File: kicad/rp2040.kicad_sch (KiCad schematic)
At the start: 0 parts

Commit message: w5500 ethernet schematic
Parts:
- added U1: RP2040, Package_DFN_QFN:QFN-56-1EP_7x7mm_P0.4mm_EP3.2x3.2mm, symbol MCU_RaspberryPi:RP2040
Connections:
- new net: U1.1 (IOVDD), U1.10 (IOVDD), U1.22 (IOVDD), U1.33 (IOVDD), U1.42 (IOVDD), U1.49 (IOVDD)
- new net: U1.23 (DVDD), U1.50 (DVDD)
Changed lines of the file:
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@@
 	(generator_version "9.0")
 	(paper "A4")
+	(symbol
+		(lib_id "MCU_RaspberryPi:RP2040")
+		(at 144.78 97.79 0)
+		(unit 1)
+		(exclude_from_sim no)
+		(in_bom yes)
+		(on_board yes)
+		(dnp no)
+		(fields_autoplaced yes)
+		(property "Reference" "U1"
+			(at 146.9233 142.24 0)
+			(effects
+				(font
+					(size 1.27 1.27)
+				)
+				(justify left)
+			)
+		)
+		(property "Value" "RP2040"
+			(at 146.9233 144.78 0)
+			(effects
+				(font
+					(size 1.27 1.27)
+				)
+				(justify left)
+			)
+		)
+		(property "Footprint" "Package_DFN_QFN:QFN-56-1EP_7x7mm_P0.4mm_EP3.2x3.2mm"
+			(at 144.78 97.79 0)
+			(effects
+				(font
+					(size 1.27 1.27)
+				)
+				(hide yes)
+			)
+		)
+		(property "Datasheet" "https://datasheets.raspberrypi.com/rp2040/rp2040-datasheet.pdf"
+			(at 144.78 97.79 0)
+			(effects
+				(font
+					(size 1.27 1.27)
+				)
+				(hide yes)
+			)
+		)
+		(property "Description" "A microcontroller by Raspberry Pi"
+			(at 144.78 97.79 0)
+			(effects
+				(font
+					(size 1.27 1.27)
+				)
+				(hide yes)
+			)
+		)
+		(pin "32"
+		)
+		(pin "12"
+		)
+		(pin "13"
+		)
+		(pin "41"
+		)
+		(pin "22"
+		)
+		(pin "9"
+		)
+		(pin "17"
+		)
+		(pin "5"
+		)
+		(pin "19"
+		)
+		(pin "11"
+		)
+		(pin "14"
+		)
+		(pin "7"
+		)
+		(pin "8"
+		)
+		(pin "16"
+		)
+		(pin "50"
+		)
+		(pin "23"
+		)
+		(pin "57"
+		)
+		(pin "4"
+		)
+		(pin "46"
+		)
+		(pin "56"
+		)
+		(pin "53"
+		)
+		(pin "55"
+		)
+		(pin "54"
+		)
+		(pin "31"
+		)
+		(pin "15"
+		)
+		(pin "29"
+		)
+		(pin "10"
+		)
+		(pin "43"
+		)
+		(pin "1"
+		)
+		(pin "28"
+		)
+		(pin "45"
+		)
+		(pin "47"
+		)
+		(pin "26"
+		)
+		(pin "52"
+		)
+		(pin "51"
+		)
+		(pin "24"
+		)
+		(pin "33"
+		)
+		(pin "36"
+		)
+		(pin "35"
+		)
+		(pin "2"
+		)
+		(pin "20"
+		)
+		(pin "21"
+		)
+		(pin "3"
+		)
+		(pin "38"
+		)
+		(pin "27"
+		)
+		(pin "37"
+		)
+		(pin "18"
+		)
+		(pin "48"
+		)
+		(pin "6"
+		)
+		(pin "39"
+		)
+		(pin "34"
+		)
+		(pin "30"
+		)
+		(pin "42"
+		)
+		(pin "44"
+		)
+		(pin "25"
+		)
+		(pin "40"
+		)
+		(pin "49"
+		)
+		(instances
+			(project ""
+				(path "/ea853fa5-7daa-4d53-920c-149f1dc74042/a778e899-dab6-488b-99d3-e495ca24ca54"
+					(reference "U1")
+					(unit 1)
+				)
+			)
+		)
+	)
 )

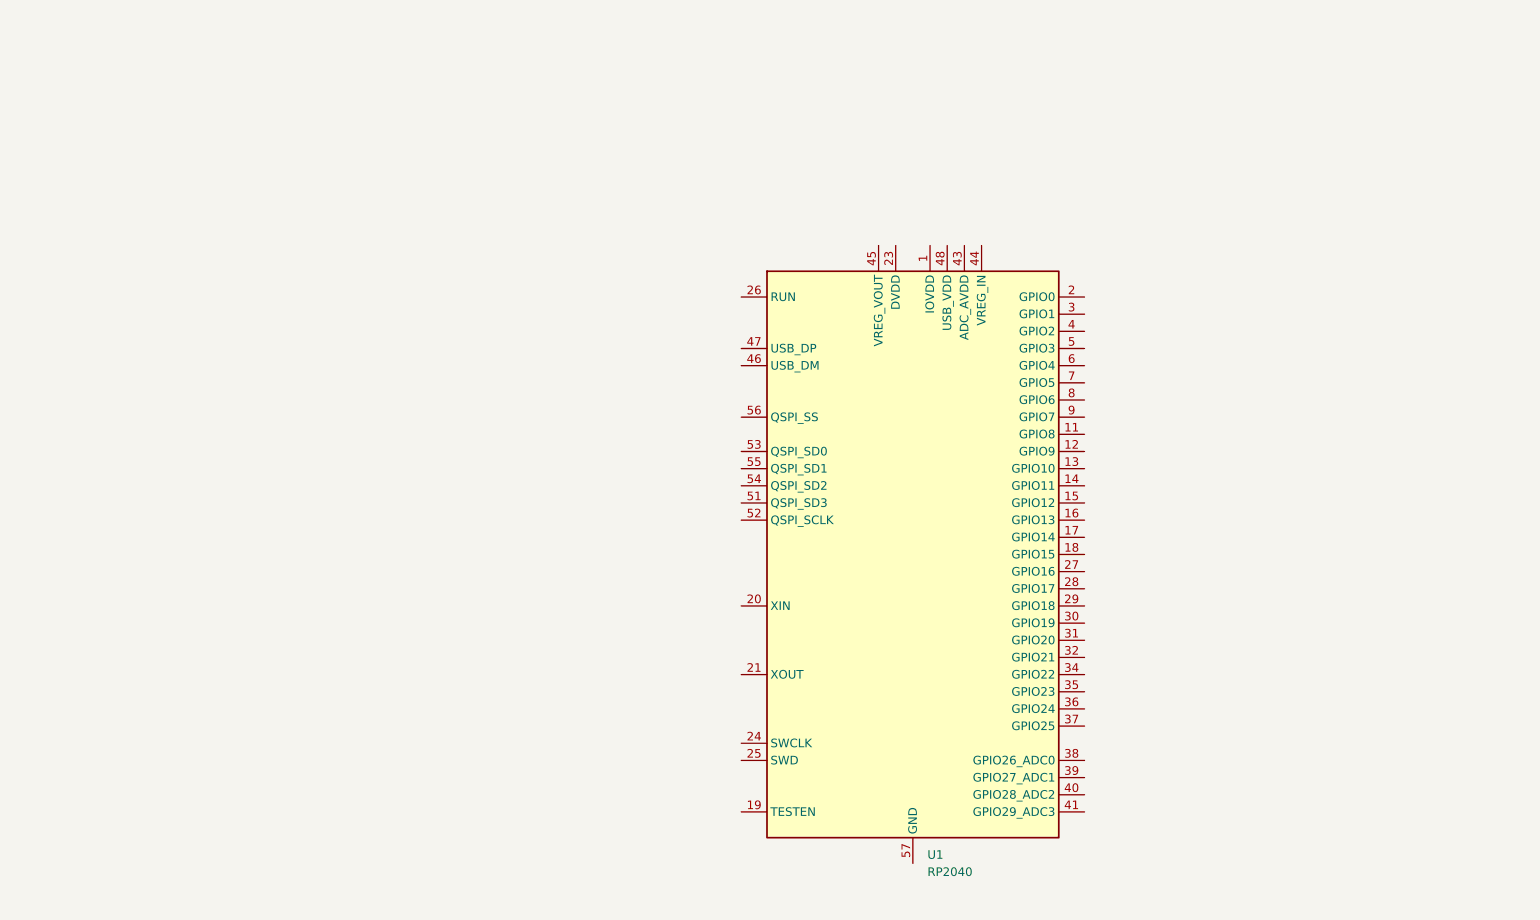
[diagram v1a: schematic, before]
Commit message: progress with minimal rp2040 setup
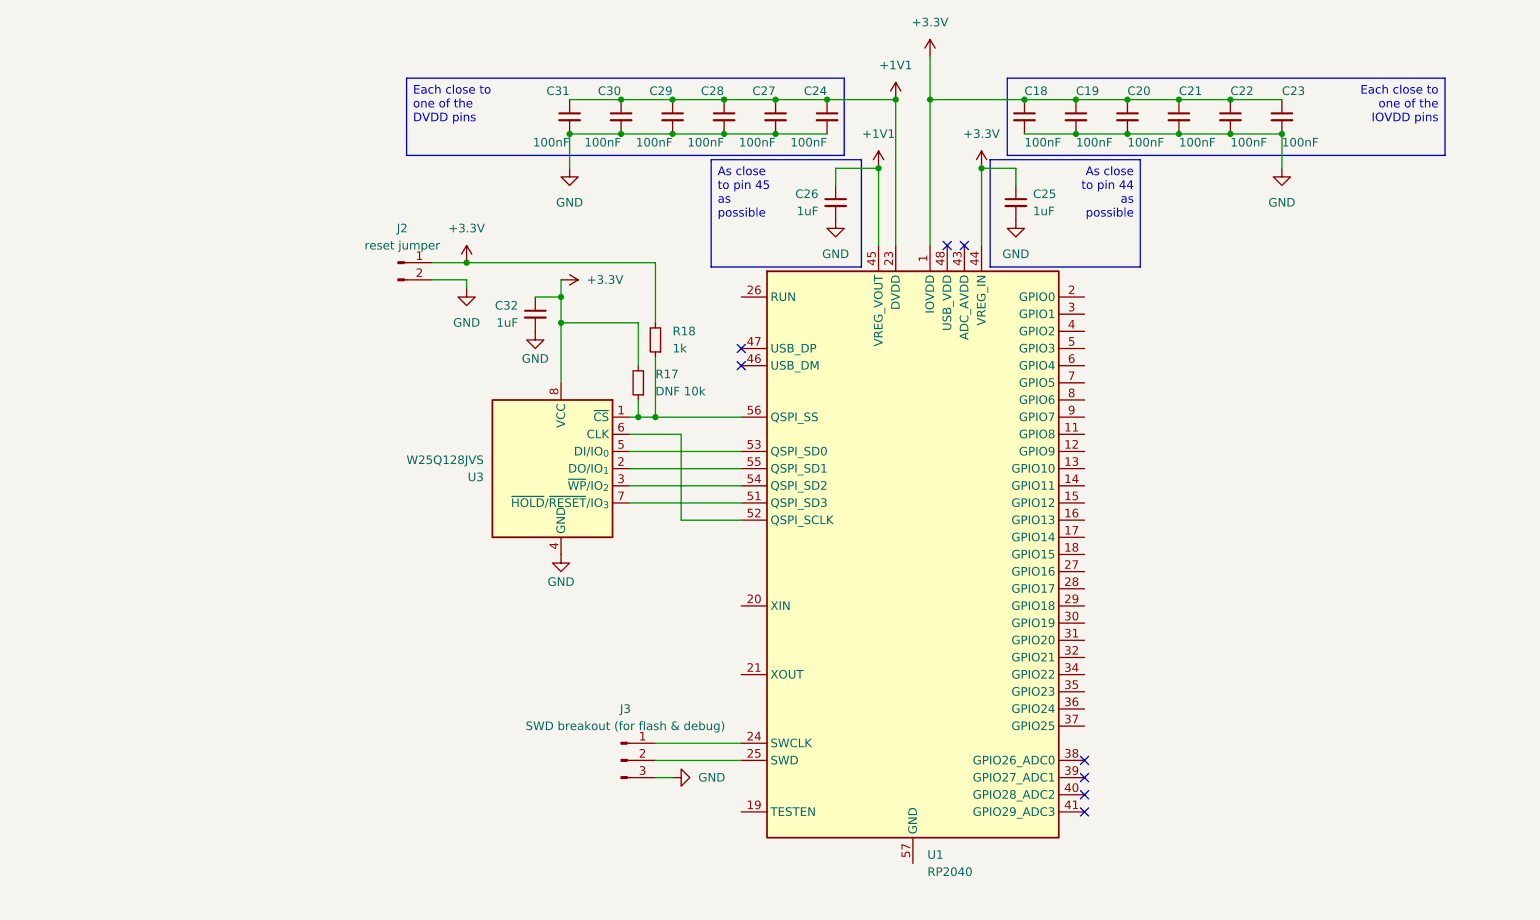
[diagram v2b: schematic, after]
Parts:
- added C18, C19, C20, C21, C22, C23, C24, C27, C28, C29, C30, C31: 100nF, symbol Device:C_Small
- added C25, C26, C32: 1uF, symbol Device:C_Small
- added J2: reset jumper, symbol Connector:Conn_01x02_Pin
- added J3: SWD breakout (for flash & debug), symbol Connector:Conn_01x03_Pin
- added R17: DNF 10k, symbol Device:R_Small
- added R18: 1k, symbol Device:R_Small
- added U3: W25Q128JVS, Package_SO:SOIC-8_5.3x5.3mm_P1.27mm, symbol Memory_Flash:W25Q128JVS
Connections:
- net +3.3V: now reaches U1.1 (IOVDD), U1.10 (IOVDD), U1.22 (IOVDD), U1.33 (IOVDD), U1.42 (IOVDD), U1.49 (IOVDD)
- net +3.3V: now also U1.44 (VREG_IN), C18.1, C19.1, C20.1, C21.1, C22.1, C23.1, C25.1, C32.1, J2.1 (Pin_1), R17.2, R18.2, U3.8 (VCC)
- net +1V1: now reaches U1.23 (DVDD), U1.50 (DVDD)
- net +1V1: now also U1.45 (VREG_VOUT), C24.1, C26.1, C27.1, C28.1, C29.1, C30.1, C31.1
- net at U1.24 (SWCLK): now also J3.1 (Pin_1)
- net at U1.25 (SWD): now also J3.2 (Pin_2)
- net at U1.51 (QSPI_SD3): now also U3.7 (~{HOLD}/~{RESET}/IO_{3})
- net at U1.52 (QSPI_SCLK): now also U3.6 (CLK)
- net at U1.53 (QSPI_SD0): now also U3.5 (DI/IO_{0})
- net at U1.54 (QSPI_SD2): now also U3.3 (~{WP}/IO_{2})
- net at U1.55 (QSPI_SD1): now also U3.2 (DO/IO_{1})
- net at U1.56 (QSPI_SS): now also R17.1, R18.1, U3.1 (~{CS})
- new net GND: C18.2, C19.2, C20.2, C21.2, C22.2, C23.2, C24.2, C25.2, C26.2, C27.2, C28.2, C29.2, C30.2, C31.2, C32.2, J2.2 (Pin_2), J3.3 (Pin_3), U3.4 (GND)
- no-connect marks 0 -> 8

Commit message: finished circuits for rp2040
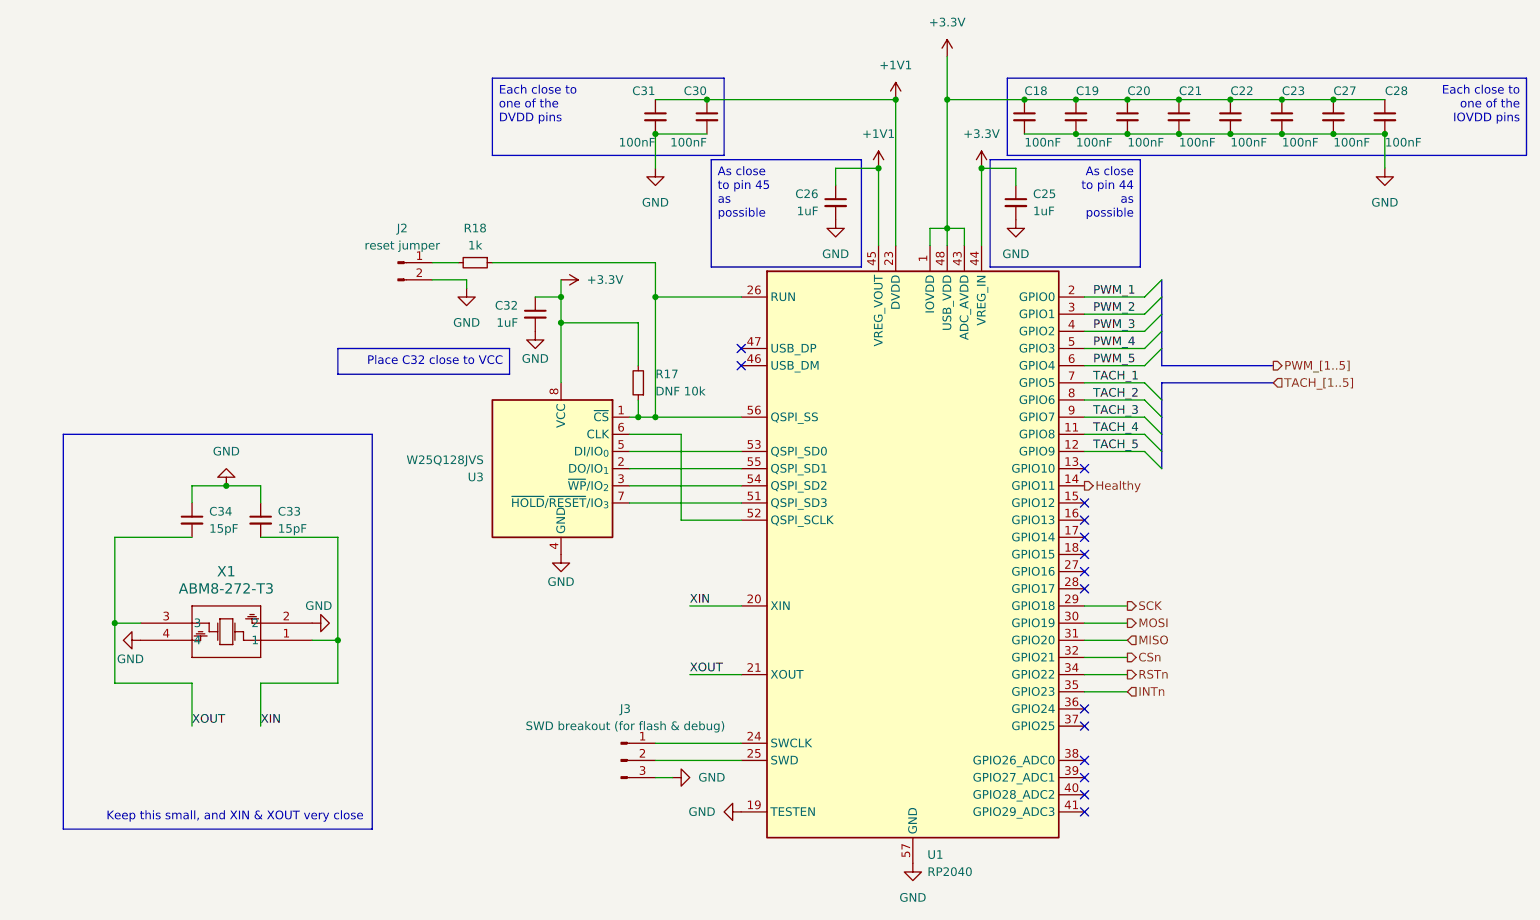
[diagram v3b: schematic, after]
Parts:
- removed C24, C29: 100nF, symbol Device:C_Small
- added C33, C34: 15pF, symbol Device:C_Small
- added X1: ABM8-272-T3, ABM8-272-T3_ABR, symbol ABM8-272-T3:ABM8-272-T3
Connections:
- net +1V1: no longer C27.1, C28.1
- net +3.3V: now also C27.1, C28.1, U1.43 (ADC_AVDD), U1.48 (USB_VDD); no longer J2.1 (Pin_1), R18.2
- net GND: now also U1.19 (TESTEN), U1.57 (GND), C33.1, C34.1, X1.2, X1.4
- net at R17.1, R18.1, U1.56 (QSPI_SS)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: now also U1.26 (RUN)
- net TACH_4: now reaches U1.11 (GPIO8)
- net TACH_5: now reaches U1.12 (GPIO9)
- net Healthy: now reaches U1.14 (GPIO11)
- net PWM_1: now reaches U1.2 (GPIO0)
- net XIN: now reaches U1.20 (XIN)
- net XIN: now also C33.2, X1.1
- net XOUT: now reaches U1.21 (XOUT)
- net XOUT: now also C34.2, X1.3
- net SCK: now reaches U1.29 (GPIO18)
- net PWM_2: now reaches U1.3 (GPIO1)
- net MOSI: now reaches U1.30 (GPIO19)
- net MISO: now reaches U1.31 (GPIO20)
- net CSn: now reaches U1.32 (GPIO21)
- net RSTn: now reaches U1.34 (GPIO22)
- net INTn: now reaches U1.35 (GPIO23)
- net PWM_3: now reaches U1.4 (GPIO2)
- net PWM_4: now reaches U1.5 (GPIO3)
- net PWM_5: now reaches U1.6 (GPIO4)
- net TACH_1: now reaches U1.7 (GPIO5)
- net TACH_2: now reaches U1.8 (GPIO6)
- net TACH_3: now reaches U1.9 (GPIO7)
- new net: J2.1 (Pin_1), R18.2
- no-connect marks 8 -> 15
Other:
- note added: "Keep this small, and XIN & XOUT very close"
- moved on the sheet: C30, C31, R18

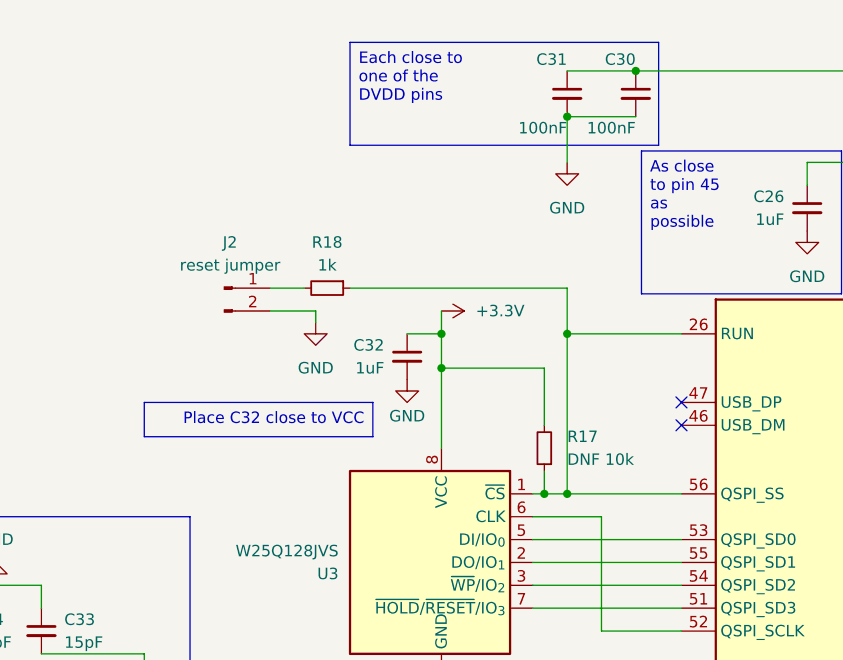
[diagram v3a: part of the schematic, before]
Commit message: bootsel not needed, only run
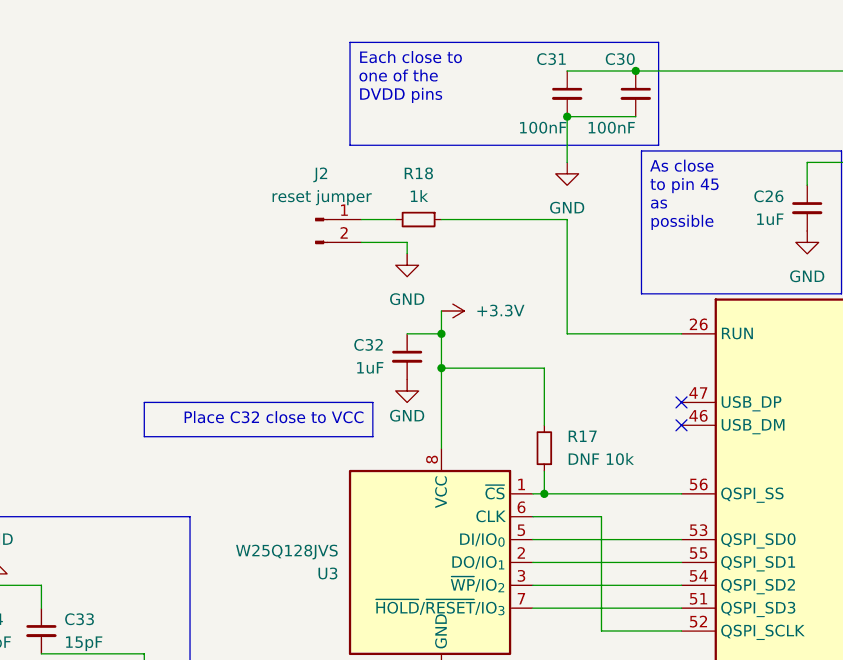
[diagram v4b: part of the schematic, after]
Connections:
- net at R17.1, U1.56 (QSPI_SS), U3.1 (~{CS}): no longer R18.1, U1.26 (RUN)
- new net: R18.1, U1.26 (RUN)
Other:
- moved on the sheet: J2, R18
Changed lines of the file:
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@@
 	)
 	(junction
-		(at 106.68 77.47)
-		(diameter 0)
-		(color 0 0 0 0)
-	)
-	(junction
-		(at 106.68 59.69)
-		(diameter 0)
-		(color 0 0 0 0)
-	)
-	(junction
 		(at 161.29 30.48)
 		(diameter 0)
@@
 	(wire
 		(pts
+			(xy 83.82 49.53) (xy 88.9 49.53)
+		)
+		(stroke
+			(width 0)
+			(type default)
+		)
+	)
+	(wire
+		(pts
 			(xy 170.18 74.93) (xy 179.07 74.93)
 		)
@@
 	(wire
 		(pts
-			(xy 73.66 57.15) (xy 78.74 57.15)
-		)
-		(stroke
-			(width 0)
-			(type default)
-		)
-	)
-	(wire
-		(pts
 			(xy 92.71 57.15) (xy 92.71 59.69)
 		)
@@
 	(wire
 		(pts
-			(xy 73.66 54.61) (xy 77.47 54.61)
-		)
-		(stroke
-			(width 0)
-			(type default)
-		)
-	)
-	(wire
-		(pts
 			(xy 48.26 95.25) (xy 59.69 95.25)
 		)
@@
 	(wire
 		(pts
-			(xy 147.32 52.07) (xy 147.32 49.53)
+			(xy 88.9 49.53) (xy 88.9 50.8)
 		)
 		(stroke
@@
 	(wire
 		(pts
-			(xy 106.68 125.73) (xy 119.38 125.73)
-		)
-		(stroke
-			(width 0)
-			(type default)
-		)
-	)
-	(wire
-		(pts
-			(xy 176.53 35.56) (xy 184.15 35.56)
+			(xy 147.32 52.07) (xy 147.32 49.53)
 		)
 		(stroke
@@
 	(wire
 		(pts
-			(xy 207.01 30.48) (xy 214.63 30.48)
+			(xy 106.68 125.73) (xy 119.38 125.73)
 		)
 		(stroke
@@
 	(wire
 		(pts
-			(xy 147.32 49.53) (xy 149.86 49.53)
+			(xy 176.53 35.56) (xy 184.15 35.56)
 		)
 		(stroke
@@
 	(wire
 		(pts
-			(xy 179.07 82.55) (xy 170.18 82.55)
+			(xy 207.01 30.48) (xy 214.63 30.48)
 		)
 		(stroke
@@
 	(wire
 		(pts
-			(xy 102.87 87.63) (xy 119.38 87.63)
+			(xy 147.32 49.53) (xy 149.86 49.53)
 		)
 		(stroke
@@
 	(wire
 		(pts
-			(xy 104.14 77.47) (xy 106.68 77.47)
+			(xy 179.07 82.55) (xy 170.18 82.55)
 		)
 		(stroke
@@
 	(wire
 		(pts
-			(xy 106.68 59.69) (xy 106.68 77.47)
+			(xy 102.87 87.63) (xy 119.38 87.63)
 		)
 		(stroke
@@
 	(wire
 		(pts
-			(xy 106.68 54.61) (xy 106.68 59.69)
+			(xy 83.82 46.99) (xy 87.63 46.99)
+		)
+		(stroke
+			(width 0)
+			(type default)
+		)
+	)
+	(wire
+		(pts
+			(xy 106.68 46.99) (xy 106.68 59.69)
 		)
 		(stroke
@@
 	(wire
 		(pts
-			(xy 78.74 57.15) (xy 78.74 58.42)
-		)
-		(stroke
-			(width 0)
-			(type default)
-		)
-	)
-	(wire
-		(pts
 			(xy 26.67 107.95) (xy 26.67 116.84)
 		)
@@
 	(wire
 		(pts
-			(xy 106.68 77.47) (xy 119.38 77.47)
+			(xy 104.14 77.47) (xy 119.38 77.47)
 		)
 		(stroke
@@
 	(wire
 		(pts
+			(xy 92.71 46.99) (xy 106.68 46.99)
+		)
+		(stroke
+			(width 0)
+			(type default)
+		)
+	)
+	(wire
+		(pts
 			(xy 142.24 30.48) (xy 142.24 52.07)
 		)
@@
 	(wire
 		(pts
-			(xy 82.55 54.61) (xy 106.68 54.61)
-		)
-		(stroke
-			(width 0)
-			(type default)
-		)
-	)
-	(wire
-		(pts
 			(xy 48.26 123.19) (xy 48.26 116.84)
 		)
@@
 	(symbol
 		(lib_id "Connector:Conn_01x02_Pin")
-		(at 68.58 54.61 0)
+		(at 78.74 46.99 0)
 		(unit 1)
 		(exclude_from_sim no)
@@
 		(dnp no)
 		(property "Reference" "J2"
-			(at 69.215 49.53 0)
+			(at 79.375 41.91 0)
 			(effects
 				(font
@@
 		)
 		(property "Value" "reset jumper"
-			(at 69.215 52.07 0)
+			(at 79.375 44.45 0)
 			(effects
 				(font
@@
 		)
 		(property "Footprint" ""
-			(at 68.58 54.61 0)
+			(at 78.74 46.99 0)
 			(effects
 				(font
@@
 		)
 		(property "Datasheet" "~"
-			(at 68.58 54.61 0)
+			(at 78.74 46.99 0)
 			(effects
 				(font
@@
 		)
 		(property "Description" "Generic connector, single row, 01x02, script generated"
-			(at 68.58 54.61 0)
+			(at 78.74 46.99 0)
 			(effects
 				(font
@@
 		)
 		(instances
-			(project ""
+			(project "rpi_fan_ctrl"
 				(path "/ea853fa5-7daa-4d53-920c-149f1dc74042/a778e899-dab6-488b-99d3-e495ca24ca54"
 					(reference "J2")
@@
 	(symbol
 		(lib_id "power:GND")
-		(at 78.74 58.42 0)
+		(at 88.9 50.8 0)
 		(unit 1)
 		(exclude_from_sim no)
@@
 		(fields_autoplaced yes)
 		(property "Reference" "#PWR08"
-			(at 78.74 64.77 0)
+			(at 88.9 57.15 0)
 			(effects
 				(font
@@
 		)
 		(property "Value" "GND"
-			(at 78.74 63.5 0)
+			(at 88.9 55.88 0)
 			(effects
 				(font
@@
 		)
 		(property "Footprint" ""
-			(at 78.74 58.42 0)
+			(at 88.9 50.8 0)
 			(effects
 				(font
@@
 		)
 		(property "Datasheet" ""
-			(at 78.74 58.42 0)
+			(at 88.9 50.8 0)
 			(effects
 				(font
@@
 		)
 		(property "Description" "Power symbol creates a global label with name \"GND\" , ground"
-			(at 78.74 58.42 0)
+			(at 88.9 50.8 0)
 			(effects
 				(font
@@
 		)
 		(instances
-			(project ""
+			(project "rpi_fan_ctrl"
 				(path "/ea853fa5-7daa-4d53-920c-149f1dc74042/a778e899-dab6-488b-99d3-e495ca24ca54"
 					(reference "#PWR08")
@@
 	(symbol
 		(lib_id "Device:R_Small")
-		(at 80.01 54.61 270)
+		(at 90.17 46.99 270)
 		(unit 1)
 		(exclude_from_sim no)
@@
 		(fields_autoplaced yes)
 		(property "Reference" "R18"
-			(at 80.01 49.53 90)
+			(at 90.17 41.91 90)
 			(effects
 				(font
@@
 		)
 		(property "Value" "1k"
-			(at 80.01 52.07 90)
+			(at 90.17 44.45 90)
 			(effects
 				(font
@@
 		)
 		(property "Footprint" ""
-			(at 80.01 54.61 0)
+			(at 90.17 46.99 0)
 			(effects
 				(font
@@
 		)
 		(property "Datasheet" "~"
-			(at 80.01 54.61 0)
+			(at 90.17 46.99 0)
 			(effects
 				(font
@@
 		)
 		(property "Description" "Resistor, small symbol"
-			(at 80.01 54.61 0)
+			(at 90.17 46.99 0)
 			(effects
 				(font
